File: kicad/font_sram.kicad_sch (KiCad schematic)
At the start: 6 parts, among them U117 74F04, U63 6116, U64 6116, U69 74F157, U70 74F157, U71 74F157

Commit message: update kicad project
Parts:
- added U65: 74LS245, Package_DIP:DIP-20_W7.62mm, symbol 74xx:74LS245
- U117: seq_coord (none) -> L20
- U63: footprint Package_DIP:DIP-24_18.0mmx34.29mm_W15.24mm -> Package_DIP:DIP-24_W15.24mm; seq_coord (none) -> I16; seq_partno (none) -> Hitachi HM6116P-3; seq_silkscreen (none) -> 6116
- U64: footprint Package_DIP:DIP-24_18.0mmx34.29mm_W15.24mm -> Package_DIP:DIP-24_W15.24mm; seq_coord (none) -> I18; seq_partno (none) -> Hitachi HM6116P-3; seq_silkscreen (none) -> 6116
- U69: seq_coord (none) -> J18
- U70: seq_coord (none) -> J19
- U71: seq_coord (none) -> J20
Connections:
- net +5V: now also U65.20 (VCC)
- net CC_D2: now also U70.3 (I1a); no longer U71.3 (I1a)
- net CC_D3: now also U70.13 (I1d); no longer U70.3 (I1a)
- net CC_D7: now also U71.3 (I1a); no longer U70.13 (I1d)
- net FD0: now also U65.16 (B2)
- net FD1: now also U65.17 (B1)
- net FD2: now also U65.18 (B0)
- net FD3: now also U65.11 (B7)
- net FD4: now also U65.12 (B6)
- net FD5: now also U65.13 (B5)
- net FD6: now also U65.14 (B4)
- net FD7: now also U65.15 (B3)
- net GND: now also U65.10 (GND)
- net XA0 renamed CPU_{A0}
- net XA1 renamed CPU_{A1}
- net XA10 renamed CPU_{A10}
- net XA11 renamed CPU_{A11}
- net XA2 renamed CPU_{A2}
- net XA3 renamed CPU_{A3}
- net XA4 renamed CPU_{A4}
- net XA5 renamed CPU_{A5}
- net XA6 renamed CPU_{A6}
- net XA7 renamed CPU_{A7}
- net XA8 renamed CPU_{A8}
- net XA9 renamed CPU_{A9}
- net ~{SRAM_{DECODE}} renamed ~{SRAM_{EN}}
- net ~{SRAM_{EN}}: now also U65.19 (CE)
- net ~{SRAM_{OE}} renamed ~{SRAM_{RD}}
- net ~{SRAM_{RD}}: now also U65.1 (A->B)
- net ~{SRAM_{WE}} renamed ~{SRAM_{WR}}
- new net XD0: U65.4 (A2)
- new net XD1: U65.3 (A1)
- new net XD2: U65.2 (A0)
- new net XD3: U65.9 (A7)
- new net XD4: U65.8 (A6)
- new net XD5: U65.7 (A5)
- new net XD6: U65.6 (A4)
- new net XD7: U65.5 (A3)
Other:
- title: (none) -> Video Unit - Font SRAM
- moved on the sheet: U117A, U63, U64, U69

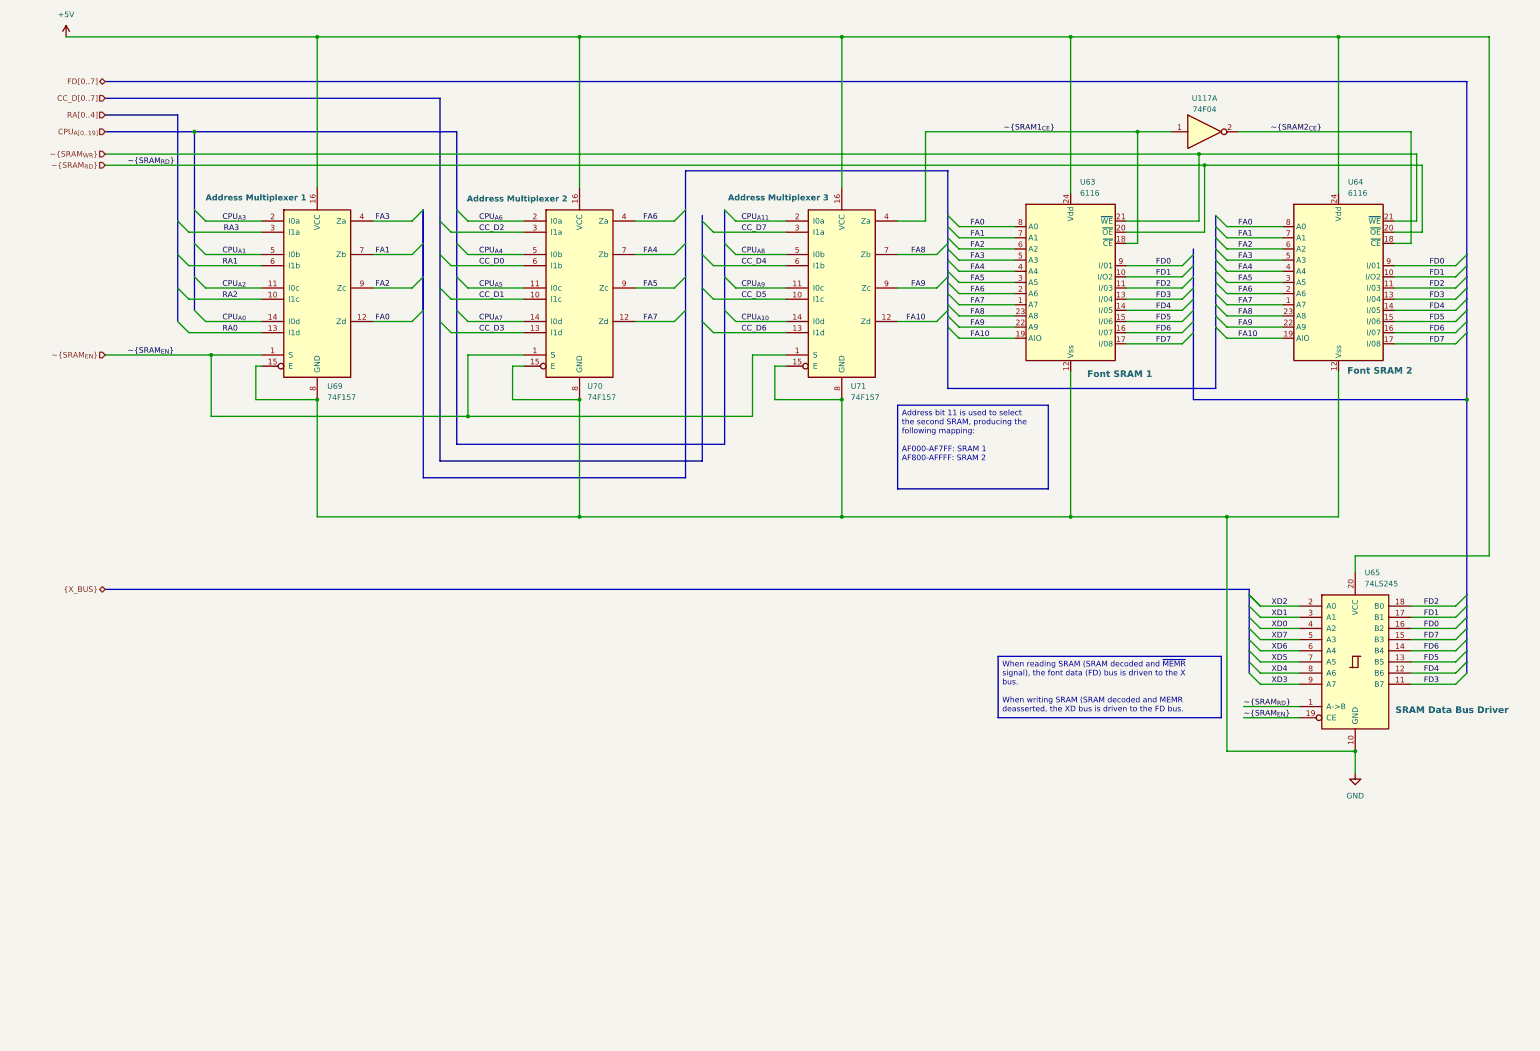
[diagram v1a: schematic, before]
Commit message: Add parallel port, game port
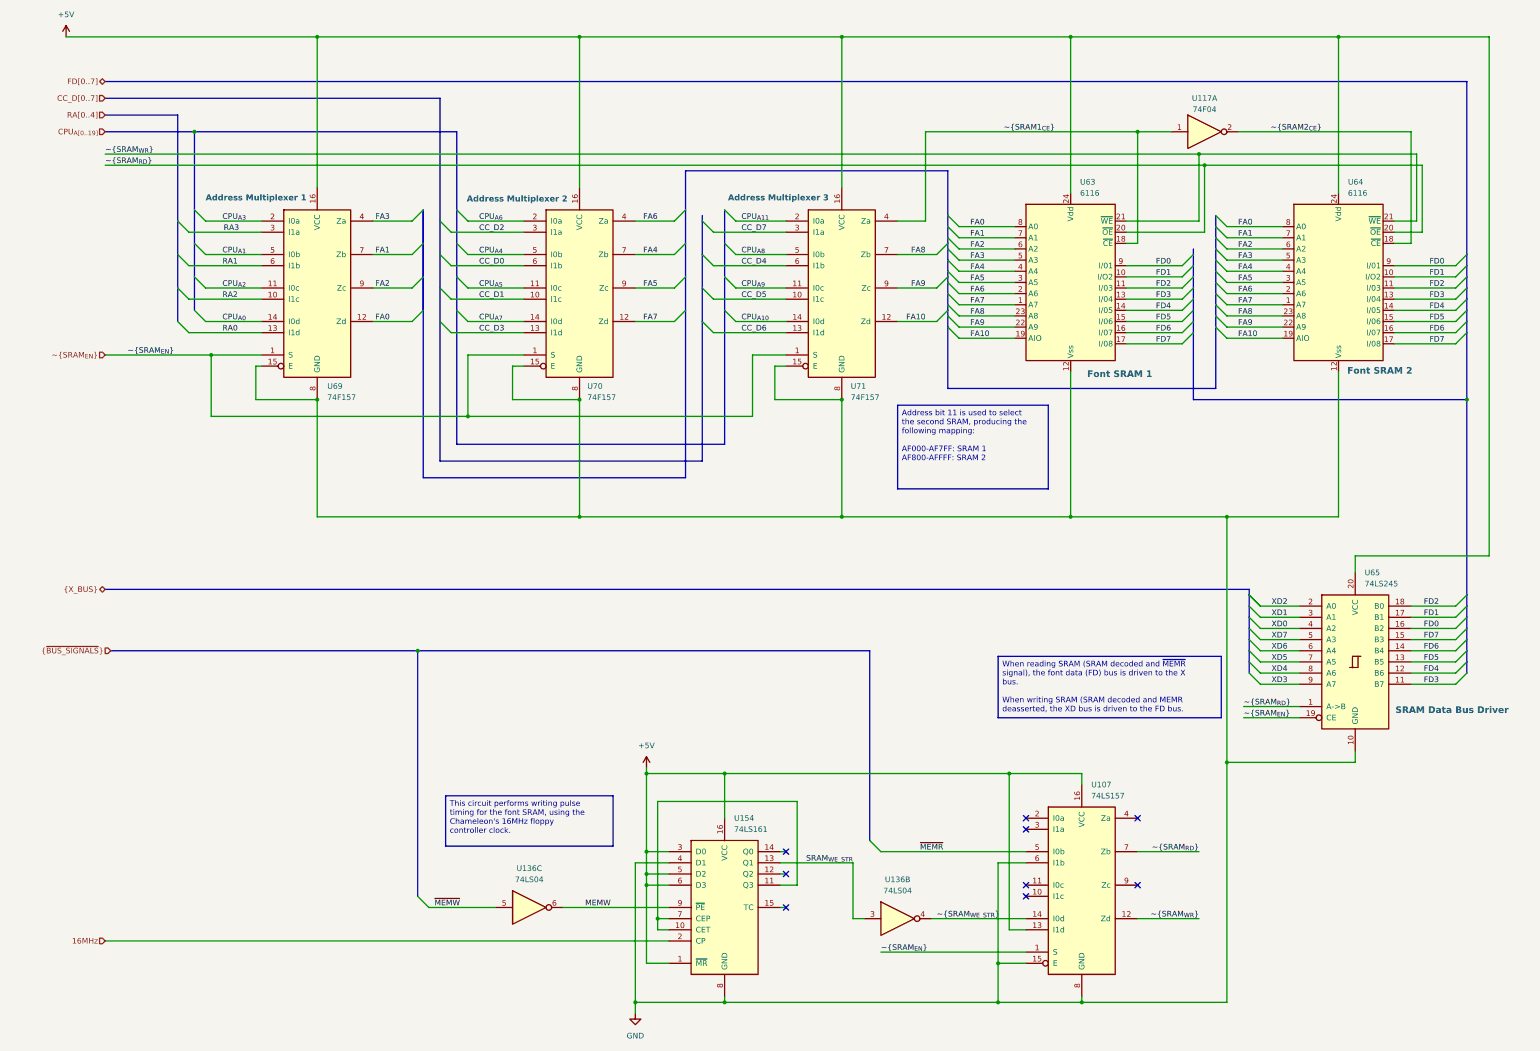
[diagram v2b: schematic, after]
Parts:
- added U107: 74LS157, Package_DIP:DIP-16_W7.62mm, symbol 74xx:74LS157
- added U136: 74LS04, Package_DIP:DIP-14_W7.62mm, symbol 74xx:74LS04
- added U154: 74LS161, Package_DIP:DIP-16_W7.62mm, symbol 74xx:74LS161
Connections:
- net +5V: now also U107.13 (I1d), U107.16 (VCC), U154.1 (~{MR}), U154.16 (VCC), U154.3 (D0), U154.5 (D2), U154.6 (D3)
- net GND: now also U107.15 (E), U107.6 (I1b), U107.8 (GND), U154.4 (D1), U154.8 (GND)
- net ~{SRAM_{EN}}: now also U107.1 (S)
- net ~{SRAM_{RD}}: now also U107.7 (Zb)
- net ~{SRAM_{WR}}: now also U107.12 (Zd)
- new net: U154.10 (CET), U154.11 (Q3), U154.7 (CEP)
- new net 16MHz: U154.2 (CP)
- new net MEMW: U136.6, U154.9 (~{PE})
- new net SRAM_{WE_STR}: U136.3, U154.13 (Q1)
- new net ~{MEMR}: U107.5 (I0b)
- new net ~{MEMW}: U136.5
- new net ~{SRAM_{WE_STR}}: U107.14 (I0d), U136.4
- no-connect marks 0 -> 9
